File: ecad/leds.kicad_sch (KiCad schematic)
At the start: 124 parts, among them U10 4069, U12 4069, U13 4069, U14 4069, U15 4069, U5 4069, U6 4069, U7 4069, U8 4069, U9 4069

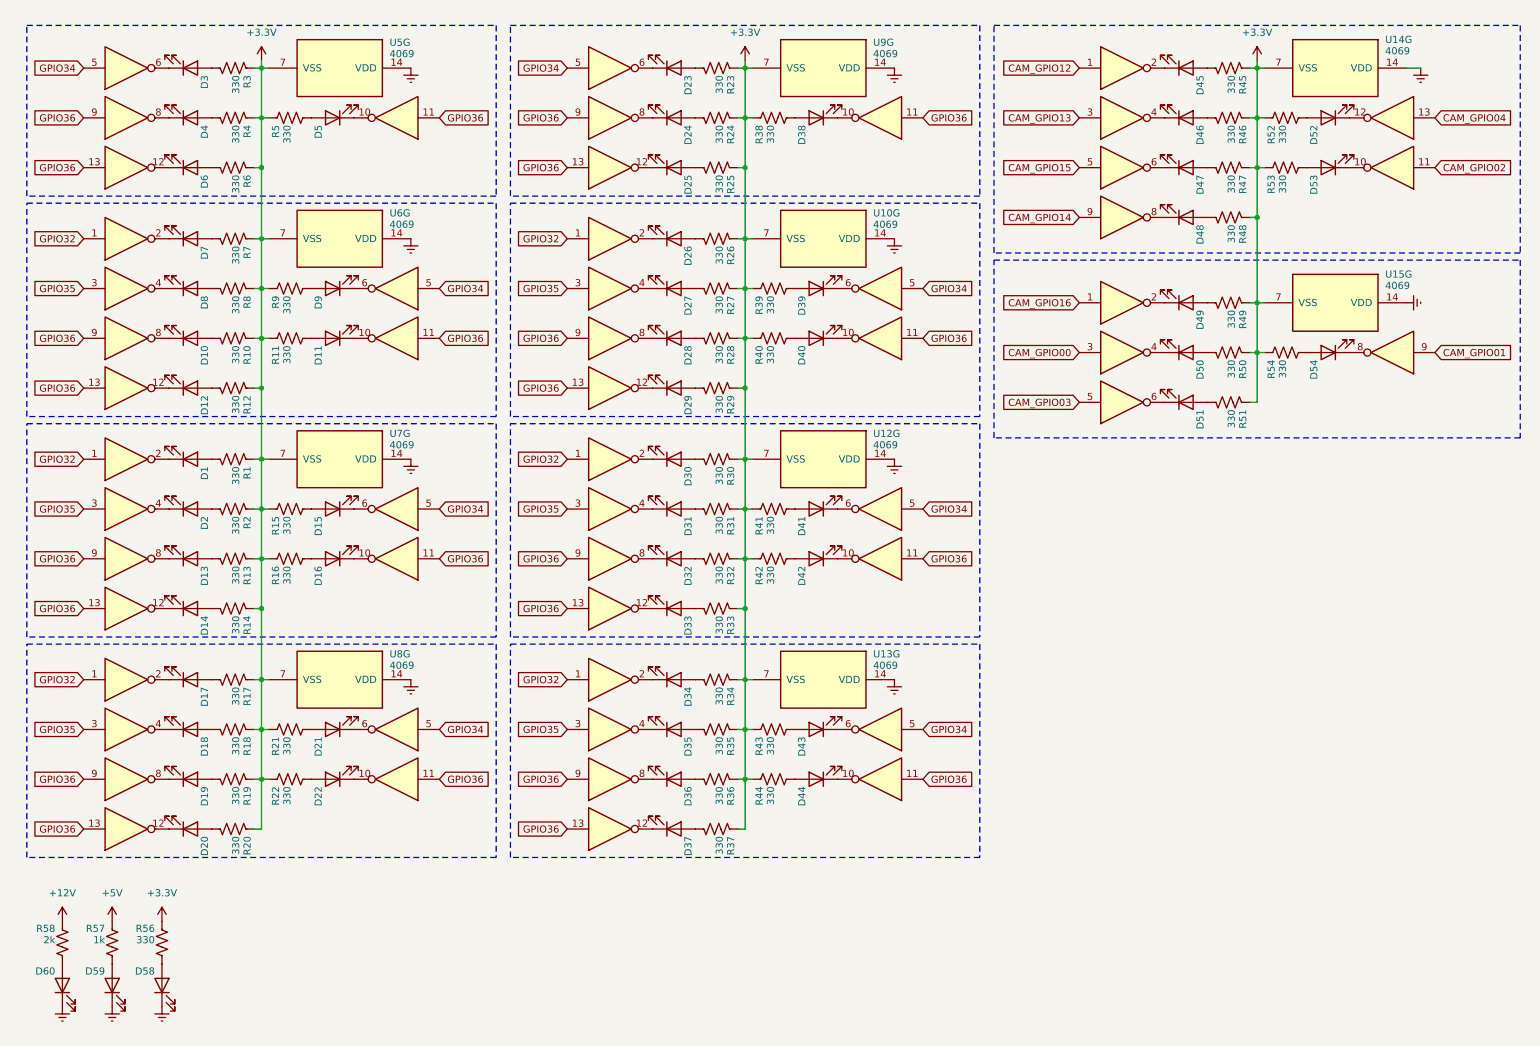
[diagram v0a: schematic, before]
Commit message: feat (ecad): start PCB design
Left header pins and LEDs connected to devkits without ground-voltage
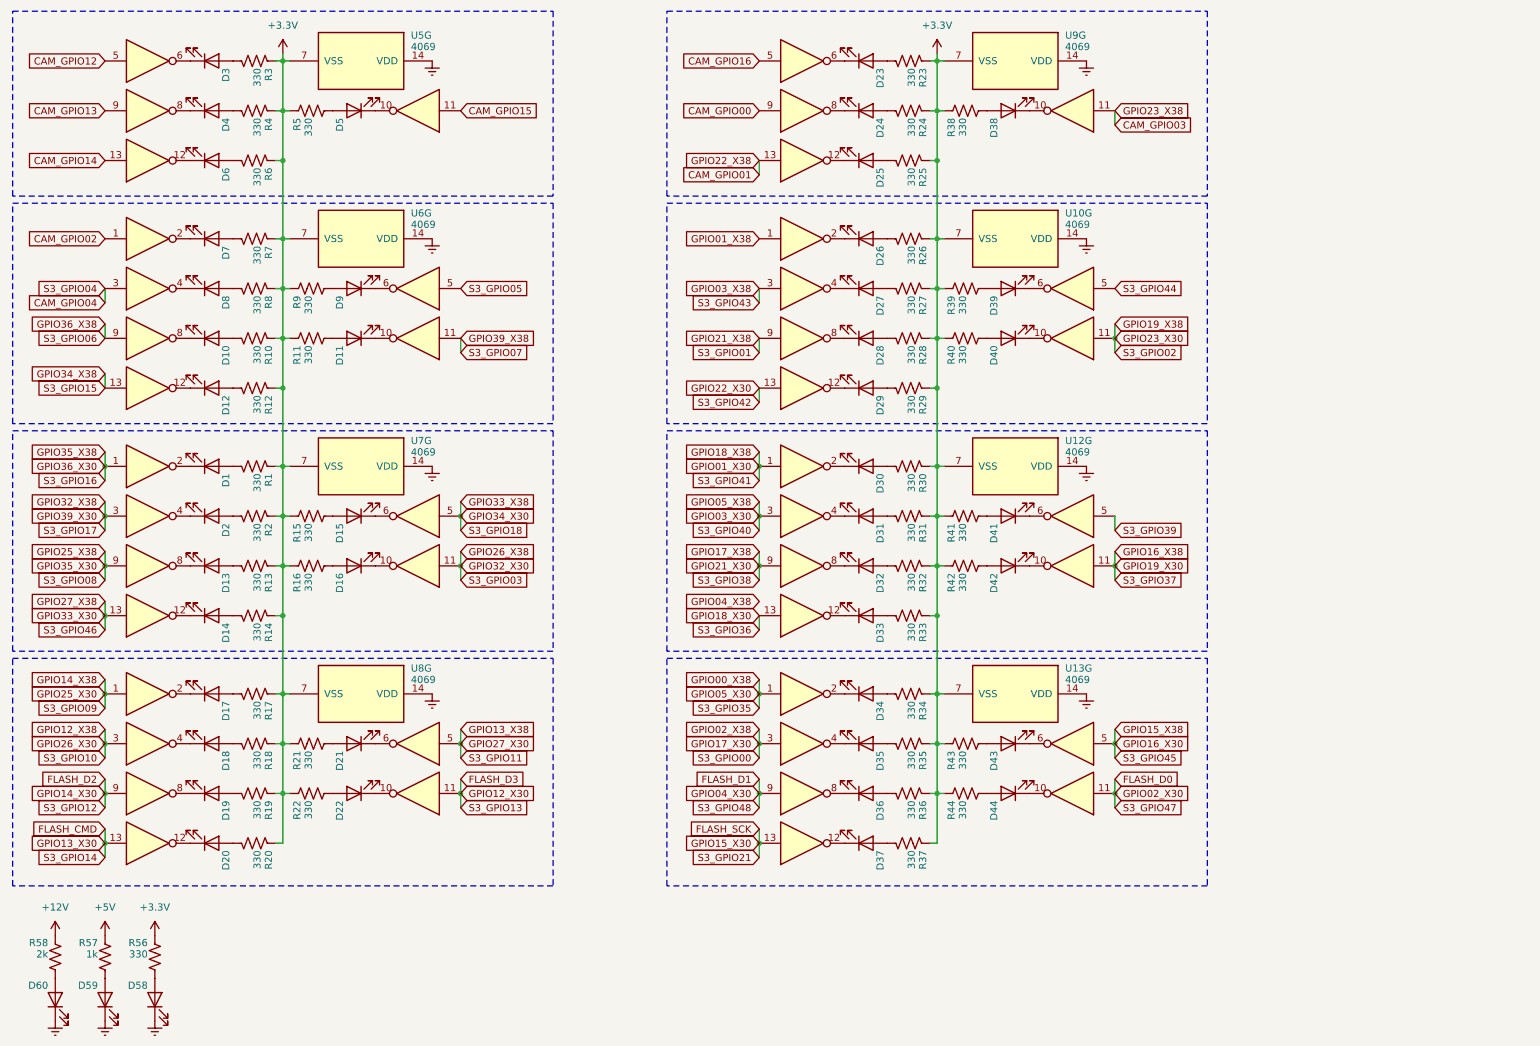
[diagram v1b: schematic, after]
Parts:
- removed D45, D46, D47, D48, D49, D50, D51, D52, D53, D54: LED, LED_SMD:LED_0805_2012Metric_Pad1.15x1.40mm_HandSolder, symbol Device:LED
- removed R45, R46, R47, R48, R49, R50, R51, R52, R53, R54: 330, Resistor_SMD:R_0805_2012Metric_Pad1.20x1.40mm_HandSolder, symbol Device:R_US
- removed U14, U15: 4069, Package_DIP:DIP-14_W8.89mm_SMDSocket_LongPads, symbol 4xxx:4069
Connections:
- net CAM_GPIO00: now also U9.9
- net CAM_GPIO01: now also U9.13
- net CAM_GPIO02: now also U6.1
- net CAM_GPIO03: now also U9.11
- net CAM_GPIO04: now also U6.3
- net CAM_GPIO12: now also U5.5
- net CAM_GPIO13: now also U5.9
- net CAM_GPIO14: now also U5.13
- net CAM_GPIO15: now also U5.11
- net CAM_GPIO16: now also U9.5
- removed net GPIO32: U10.1, U12.1, U13.1, U6.1, U7.1, U8.1
- removed net GPIO34: U10.5, U12.5, U13.5, U5.5, U6.5, U7.5, U8.5, U9.5
- removed net GPIO35: U10.3, U12.3, U13.3, U6.3, U7.3, U8.3
- removed net GPIO36: U10.11, U10.13, U10.9, U12.11, U12.13, U12.9, U13.11, U13.13, U13.9, U5.11, U5.13, U5.9, U6.11, U6.13, U6.9, U7.11, U7.13, U7.9, U8.11, U8.13, U8.9, U9.11, U9.13, U9.9
- new net FLASH_CMD: U8.13
- new net FLASH_D0: U13.11
- new net FLASH_D1: U13.9
- new net FLASH_D2: U8.9
- new net FLASH_D3: U8.11
- new net FLASH_SCK: U13.13
- new net GPIO00_X38: U13.1
- new net GPIO01_X30: U12.1
- new net GPIO01_X38: U10.1
- new net GPIO02_X38: U13.3
- new net GPIO03_X30: U12.3
- new net GPIO03_X38: U10.3
- new net GPIO12_X38: U8.3
- new net GPIO13_X38: U8.5
- new net GPIO14_X38: U8.1
- new net GPIO15_X38: U13.5
- new net GPIO16_X38: U12.11
- new net GPIO17_X38: U12.9
- new net GPIO18_X30: U12.13
- new net GPIO19_X38: U10.11
- new net GPIO21_X38: U10.9
- new net GPIO22_X30: U10.13
- new net GPIO25_X38: U7.9
- new net GPIO26_X38: U7.11
- new net GPIO27_X38: U7.13
- new net GPIO32_X38: U7.3
- new net GPIO33_X38: U7.5
- new net GPIO34_X38: U6.13
- new net GPIO35_X38: U7.1
- new net GPIO36_X38: U6.9
- new net GPIO39_X38: U6.11
- new net S3_GPIO05: U6.5
- new net S3_GPIO39: U12.5
- new net S3_GPIO44: U10.5
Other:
- moved on the sheet: D1, D10, D11, D12, D13, D14, D15, D16, D17, D18, D19, D2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

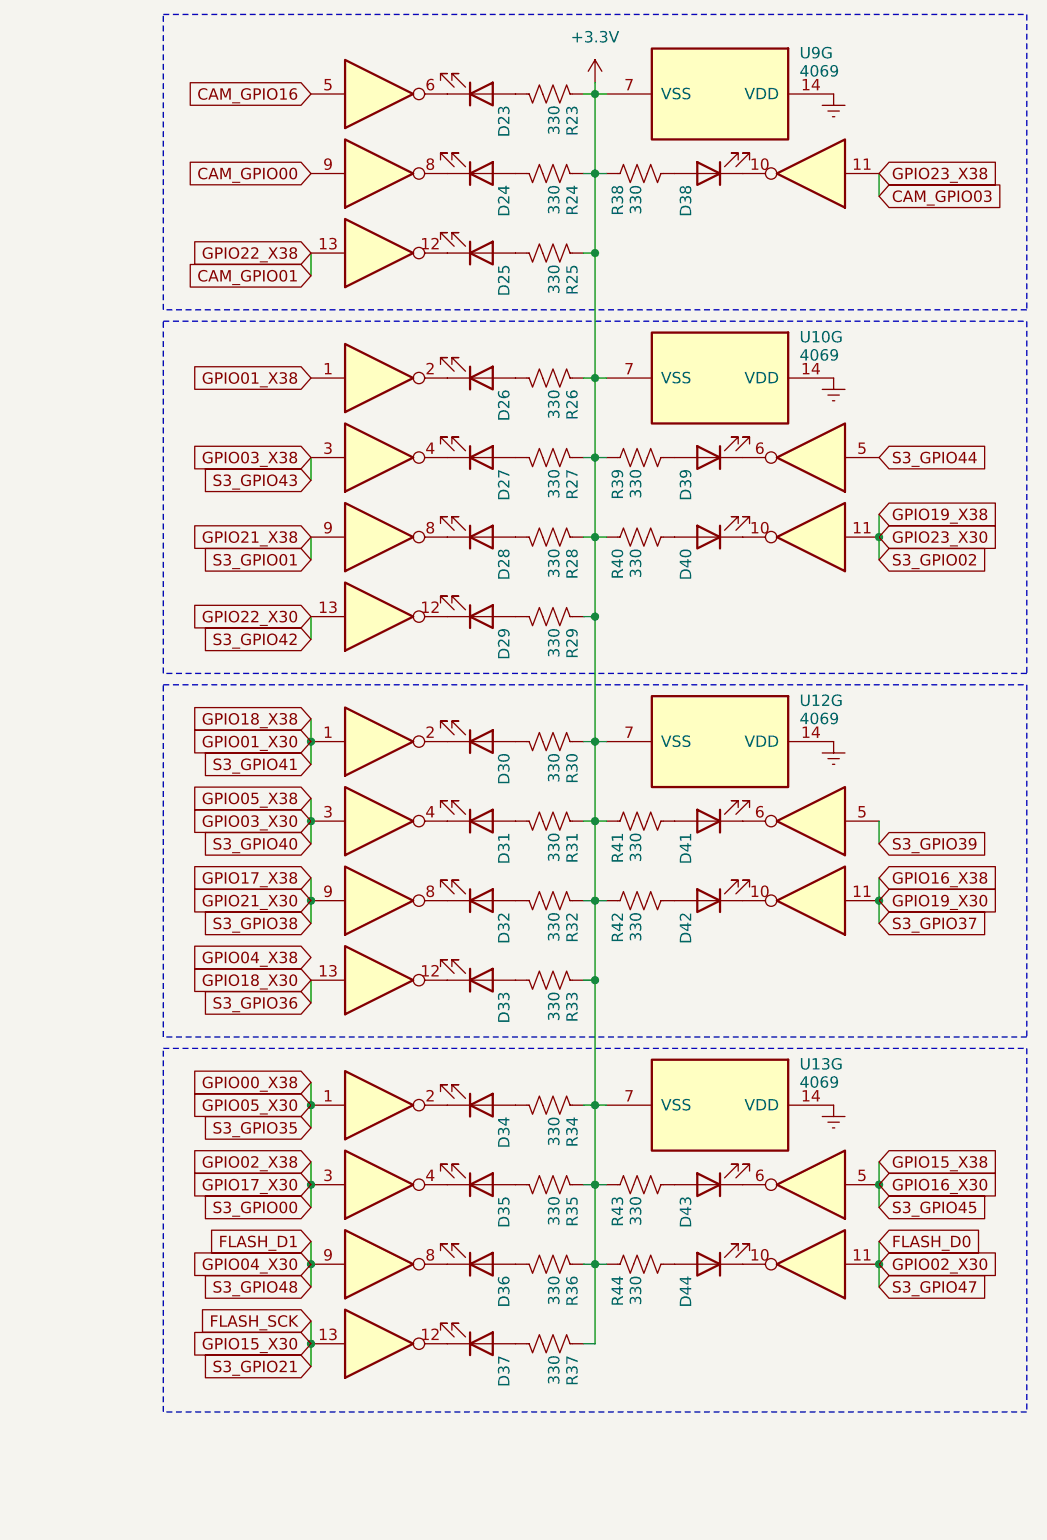
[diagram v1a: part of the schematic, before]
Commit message: feat (ecad): update PCB design
header pins and LEDs connected to devkits without ground-voltage
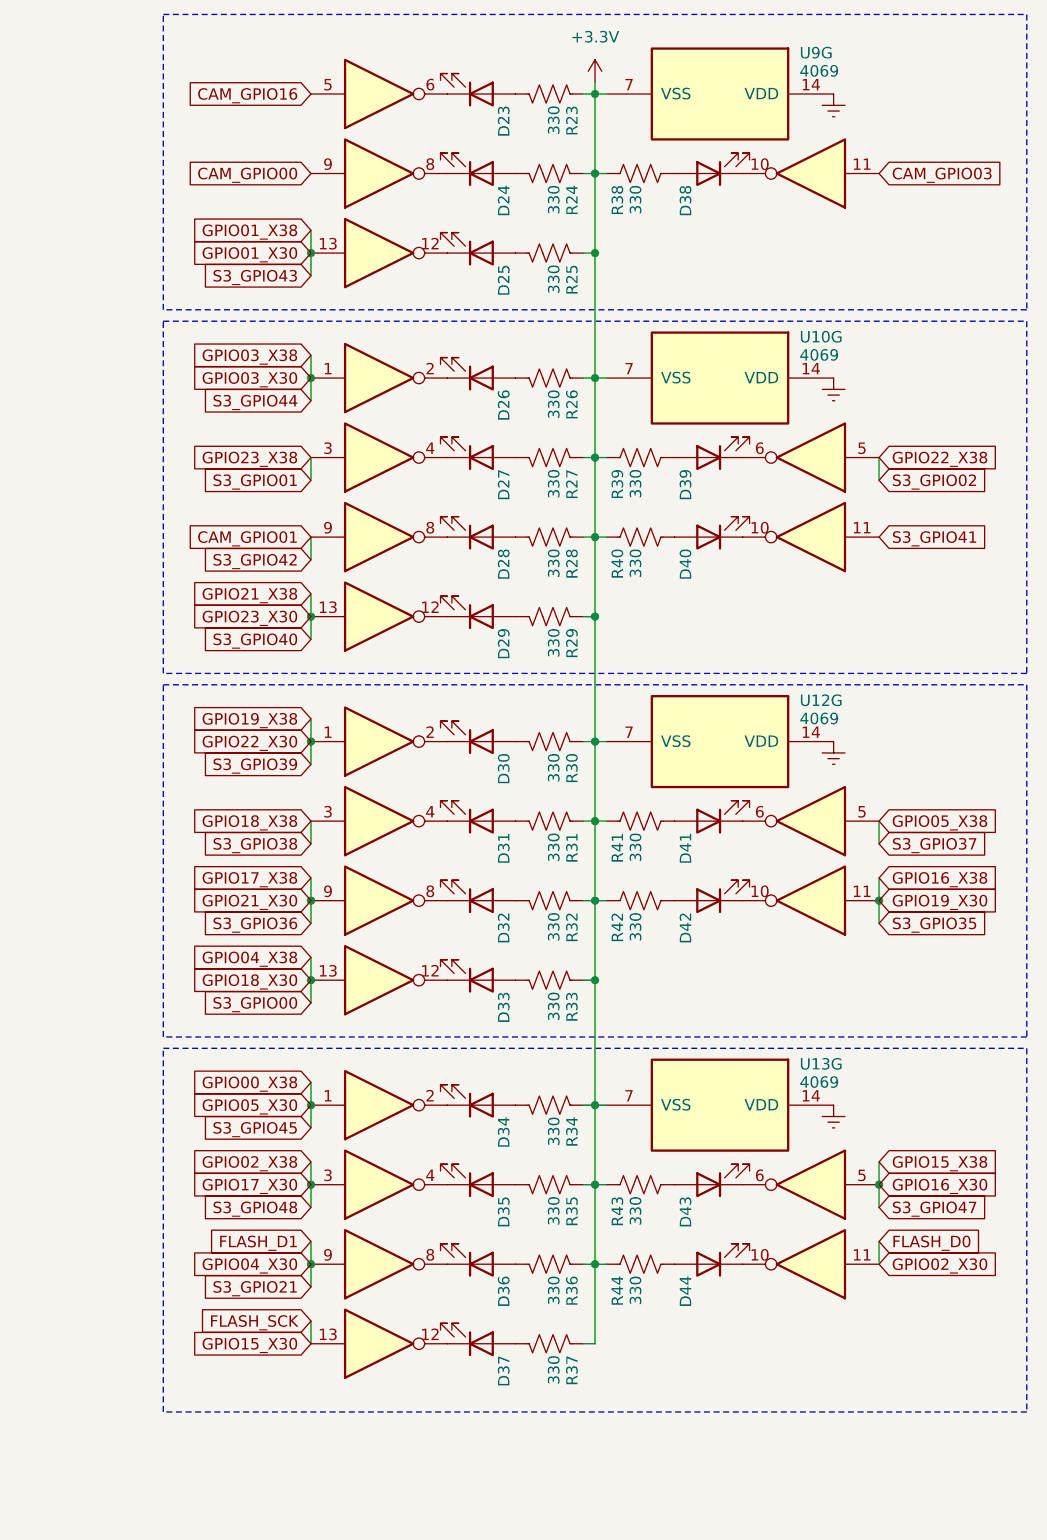
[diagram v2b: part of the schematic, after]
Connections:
- net GPIO01_X38 is gone; now on net GPIO03_X30: U10.1
- net GPIO18_X30 is gone; now on net GPIO04_X38: U12.13
- net GPIO22_X30 is gone; now on net GPIO21_X38: U10.13
- net CAM_GPIO01: now also U10.9; no longer U9.13
- net GPIO01_X30: now also U9.13; no longer U12.1
- net GPIO03_X30: no longer U12.3
- net GPIO19_X38: now also U12.1; no longer U10.11
- net GPIO21_X38: no longer U10.9
- net GPIO03_X38 renamed GPIO23_X38
- net S3_GPIO39 renamed GPIO05_X38
- net S3_GPIO44 renamed GPIO22_X38
- new net GPIO18_X38: U12.3
- new net S3_GPIO41: U10.11
